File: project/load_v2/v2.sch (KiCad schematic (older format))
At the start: 42 parts, among them P1 CONN_01X02, P2 NGUON, P3 SAC, P4 12N60, P5 CONN_01X02, P6 CONN_01X08, U1 LM7812, U2 7805, U3 ICL7660, U4 TL431

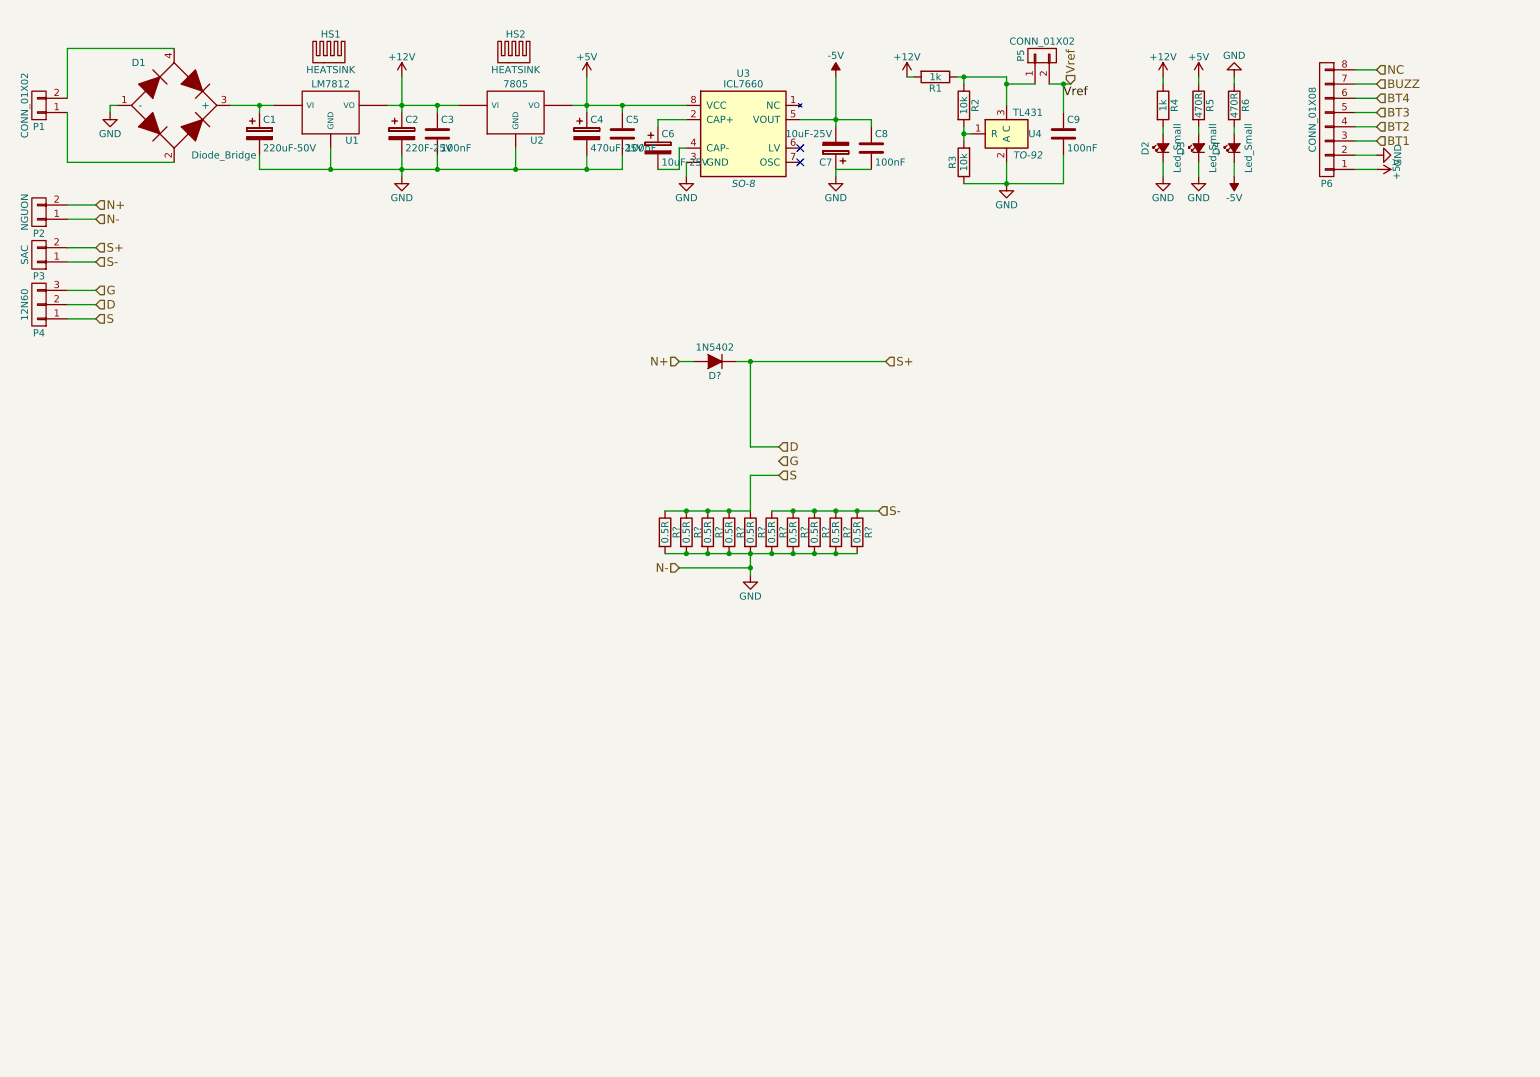
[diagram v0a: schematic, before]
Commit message: schema_load_v2
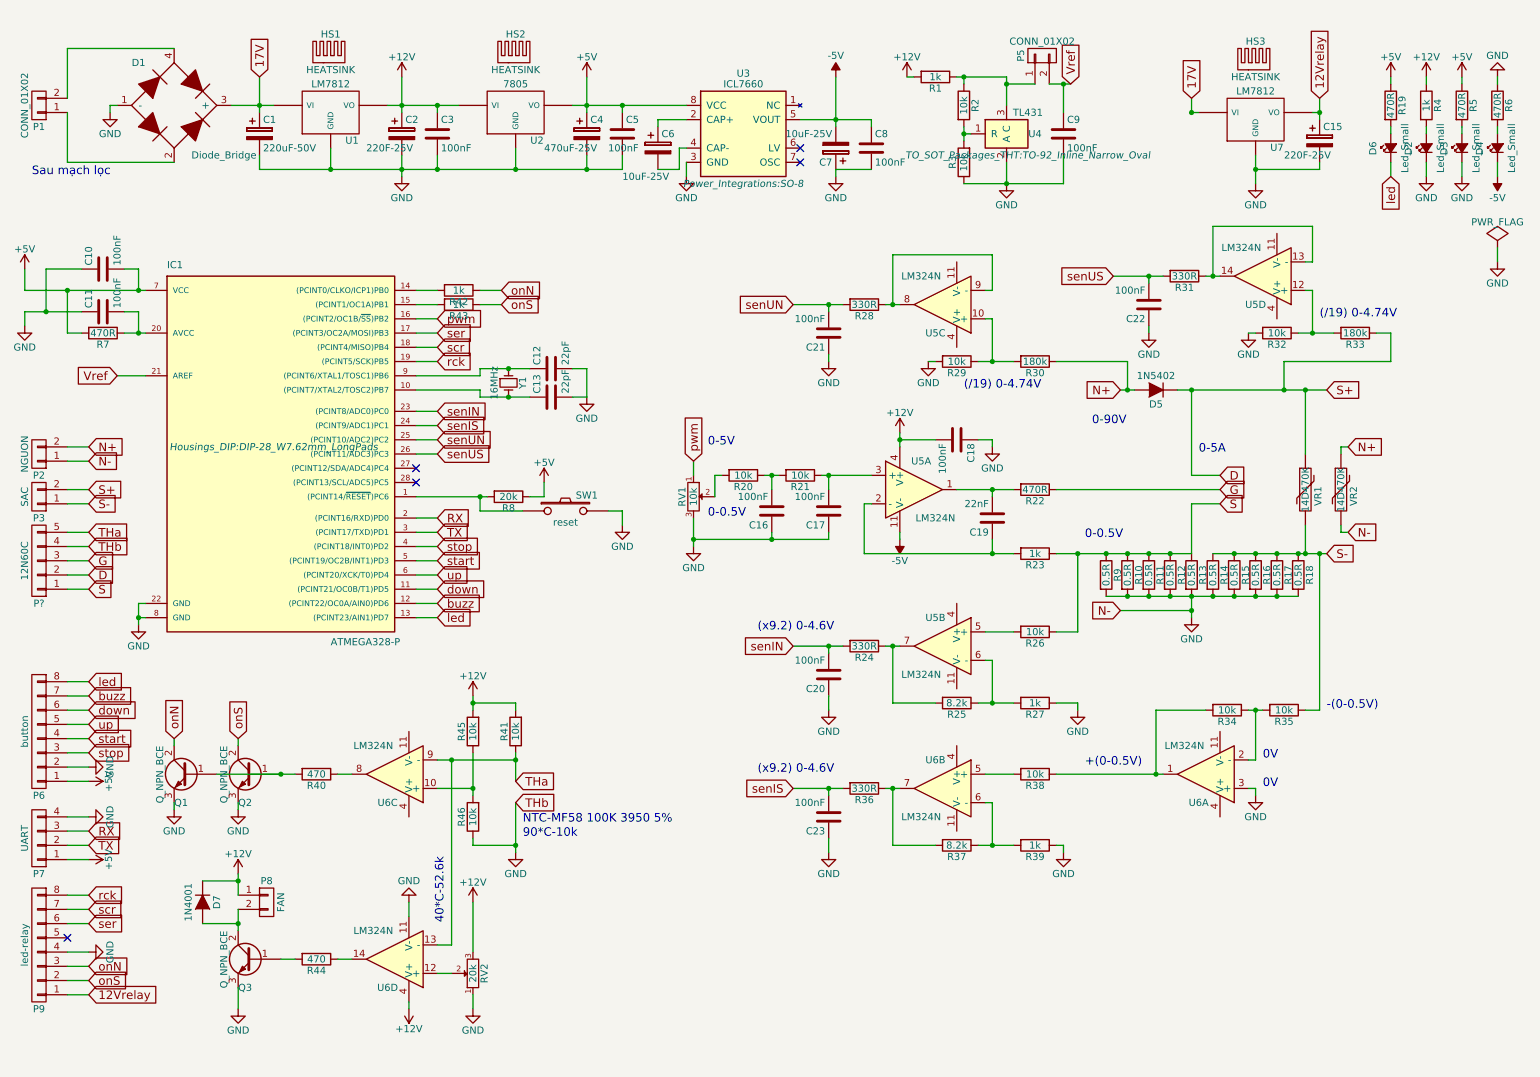
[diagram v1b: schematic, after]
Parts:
- removed P4: 12N60, symbol CONN_01X03
- added C10, C11, C16, C17, C18, C20, C21, C22, C23: 100nF, symbol C
- added C12, C13: 22pF, symbol C
- added C15: 220F-25V, symbol CP
- added C19: 22nF, symbol C
- added D6: Led_Small, symbol Led_Small
- added D7: 1N4001, symbol D
- added HS3: HEATSINK, symbol HEATSINK
- added IC1: ATMEGA328-P, Housings_DIP:DIP-28_W7.62mm_LongPads, symbol ATMEGA328-P
- added P7: UART, symbol CONN_01X04
- added P8: FAN, symbol CONN_01X02
- added P9: led-relay, Socket_Strips:Socket_Strip_Straight_1x08, symbol CONN_01X08
- added P?: 12N60C, symbol CONN_01X05
- added Q1, Q2, Q3: Q_NPN_BCE, symbol Q_NPN_BCE
- added R19, R22, R7: 470R, symbol R
- added R20, R21, R26, R29, R32, R34, R35, R38, R41, R45, R46: 10k, symbol R
- added R23, R27, R39, R42, R43: 1k, symbol R
- added R24, R28, R31, R36: 330R, symbol R
- added R25, R37: 8.2k, symbol R
- added R30, R33: 180k, symbol R
- added R40, R44: 470, symbol R
- added R8: 20k, symbol R
- added RV1: 10k, symbol POT
- added RV2: 20k, symbol POT
- added SW1: reset, symbol SW_PUSH
- added U5, U6: LM324N, symbol LM324N
- added U7: LM7812, symbol LM7812
- added VR1, VR2: 14D470K, symbol VR
- added Y1: 16MHz, Crystals:Crystal_HC52-U_Vertical, symbol Crystal_Small
- P6: value CONN_01X08 -> button; footprint (none) -> Socket_Strips:Socket_Strip_Straight_1x08
- U3: footprint SO-8 -> Power_Integrations:SO-8
- U4: footprint TO-92 -> TO_SOT_Packages_THT:TO-92_Inline_Narrow_Oval
- gave numbers to parts that had none: 11
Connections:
- net +12V: now also C18.2, D7.1 (K), P8.1 (P1), R41.2, R45.2, RV2.3, U5.4 (V+), U6.4 (V+)
- net +5V: now also C10.2, IC1.7 (VCC), P7.1 (P1), R19.1, R7.2, R8.1
- net -5V: now also U5.11 (V-)
- net D: now also P?.2 (P2), R33.1, VR1.1
- net G: now also P?.3 (P3), R22.1
- net GND: now also C10.1, C11.1, C12.2, C13.2, C15.2, C16.1, C17.1, C18.1, C20.1, C21.1, C22.1, C23.1, IC1.22 (GND), IC1.8 (GND), P7.4 (P4), P9.4 (P4), P?.4 (P4), Q1.3 (E), Q2.3 (E), Q3.3 (E), R27.1, R29.2, R32.2, R39.1, R46.1, RV1.3, RV2.1, SW1.2, U6.11 (V-), U6.3 (+), U7.GND, VR2.2
- net N+: now also R30.1, VR2.1
- net S: now also P?.1 (P1), R23.1, R26.1
- net S-: now also R35.1, VR1.2
- net Vref: now also IC1.21 (AREF)
- net 17V: now reaches C1.1, D1.3 (+), U1.VI
- net 17V: now also U7.VI
- net BT1 renamed stop
- net stop: now also IC1.4 ((PCINT18/INT0)PD2)
- net BT2 renamed start
- net start: now also IC1.5 ((PCINT19/OC2B/INT1)PD3)
- net BT3 renamed up
- net up: now also IC1.6 ((PCINT20/XCK/T0)PD4)
- net BT4 renamed down
- net down: now also IC1.11 ((PCINT21/OC0B/T1)PD5)
- net BUZZ renamed buzz
- net buzz: now also IC1.12 ((PCINT22/OC0A/AIN0)PD6)
- net NC renamed led
- net led: now also D6.1 (K), IC1.13 ((PCINT23/AIN1)PD7)
- new net: IC1.1 ((PCINT14/~RESET~)PC6), R8.2, SW1.1
- new net: C13.1, IC1.10 ((PCINT7/XTAL2/TOSC2)PB7), Y1.2
- new net: IC1.14 ((PCINT0/CLKO/ICP1)PB0), R42.2
- new net: IC1.15 ((PCINT1/OC1A)PB1), R43.2
- new net: C11.2, IC1.20 (AVCC), R7.1
- new net: C12.1, IC1.9 ((PCINT6/XTAL1/TOSC1)PB6), Y1.1
- new net: D6.2 (A), R19.2
- new net: C19.2, R22.2, U5.1
- new net: C19.1, R23.2, U5.2 (-)
- new net: C17.2, R21.1, U5.3 (+)
- new net: R26.2, U5.5 (+)
- new net: R25.1, R27.2, U5.6 (-)
- new net: R24.1, R25.2, U5.7
- new net: R29.1, R30.2, U5.10 (+)
- new net: R28.1, U5.8, U5.9 (-)
- new net: R32.1, R33.2, U5.12 (+)
- new net: R31.1, U5.13 (-), U5.14
- new net: R34.2, R38.1, U6.1
- new net: R34.1, R35.2, U6.2 (-)
- new net: R38.2, U6.5 (+)
- new net: R37.1, R39.2, U6.6 (-)
- new net: R36.1, R37.2, U6.7
- new net: R45.1, R46.2, U6.10 (+)
- new net: R40.1, U6.8
- new net: RV2.2, U6.12 (+)
- new net: R44.1, U6.14
- new net: R20.2, RV1.2
- new net: C16.2, R20.1, R21.2
- new net: Q1.1 (B), Q2.1 (B), R40.2
- new net: Q3.1 (B), R44.2
- new net: D7.2 (A), P8.2 (P2), Q3.2 (C)
- new net 12Vrelay: C15.1, P9.1 (P1), U7.VO
- new net RX: IC1.2 ((PCINT16/RXD)PD0), P7.3 (P3)
- new net THa: P?.5 (P5), R41.1, U6.13 (-), U6.9 (-)
- new net TX: IC1.3 ((PCINT17/TXD)PD1), P7.2 (P2)
- new net onN: P9.3 (P3), Q1.2 (C), R42.1
- new net onS: P9.2 (P2), Q2.2 (C), R43.1
- new net pwm: IC1.16 ((PCINT2/OC1B/~SS~)PB2), RV1.1
- new net rck: IC1.19 ((PCINT5/SCK)PB5), P9.8 (P8)
- new net scr: IC1.18 ((PCINT4/MISO)PB4), P9.7 (P7)
- new net senIN: C20.2, IC1.23 ((PCINT8/ADC0)PC0), R24.2
- new net senIS: C23.2, IC1.24 ((PCINT9/ADC1)PC1), R36.2
- new net senUN: C21.2, IC1.25 ((PCINT10/ADC2)PC2), R28.2
- new net senUS: C22.2, IC1.26 ((PCINT11/ADC3)PC3), R31.2
- new net ser: IC1.17 ((PCINT3/OC2A/MOSI)PB3), P9.6 (P6)
- no-connect marks 2 -> 5
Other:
- note added: "(/19) 0-4.74V"
- note added: "(x9.2) 0-4.6V"
- note added: "+(0-0.5V)"
- note added: "-(0-0.5V)"
- note added: "0-0.5V"
- note added: "0-5A"
- note added: "0-5V"
- note added: "0-90V"
- note added: "0V"
- note added: "40*C-52.6k"
- note added: "90*C-10k"
- note added: "NTC-MF58 100K 3950 5%"
- note added: "Sau mạch lọc"
- moved on the sheet: D2, D3, D4, D5, P2, P3, P6, R10, R11, R12, R13, R14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

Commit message: schema_load_v2
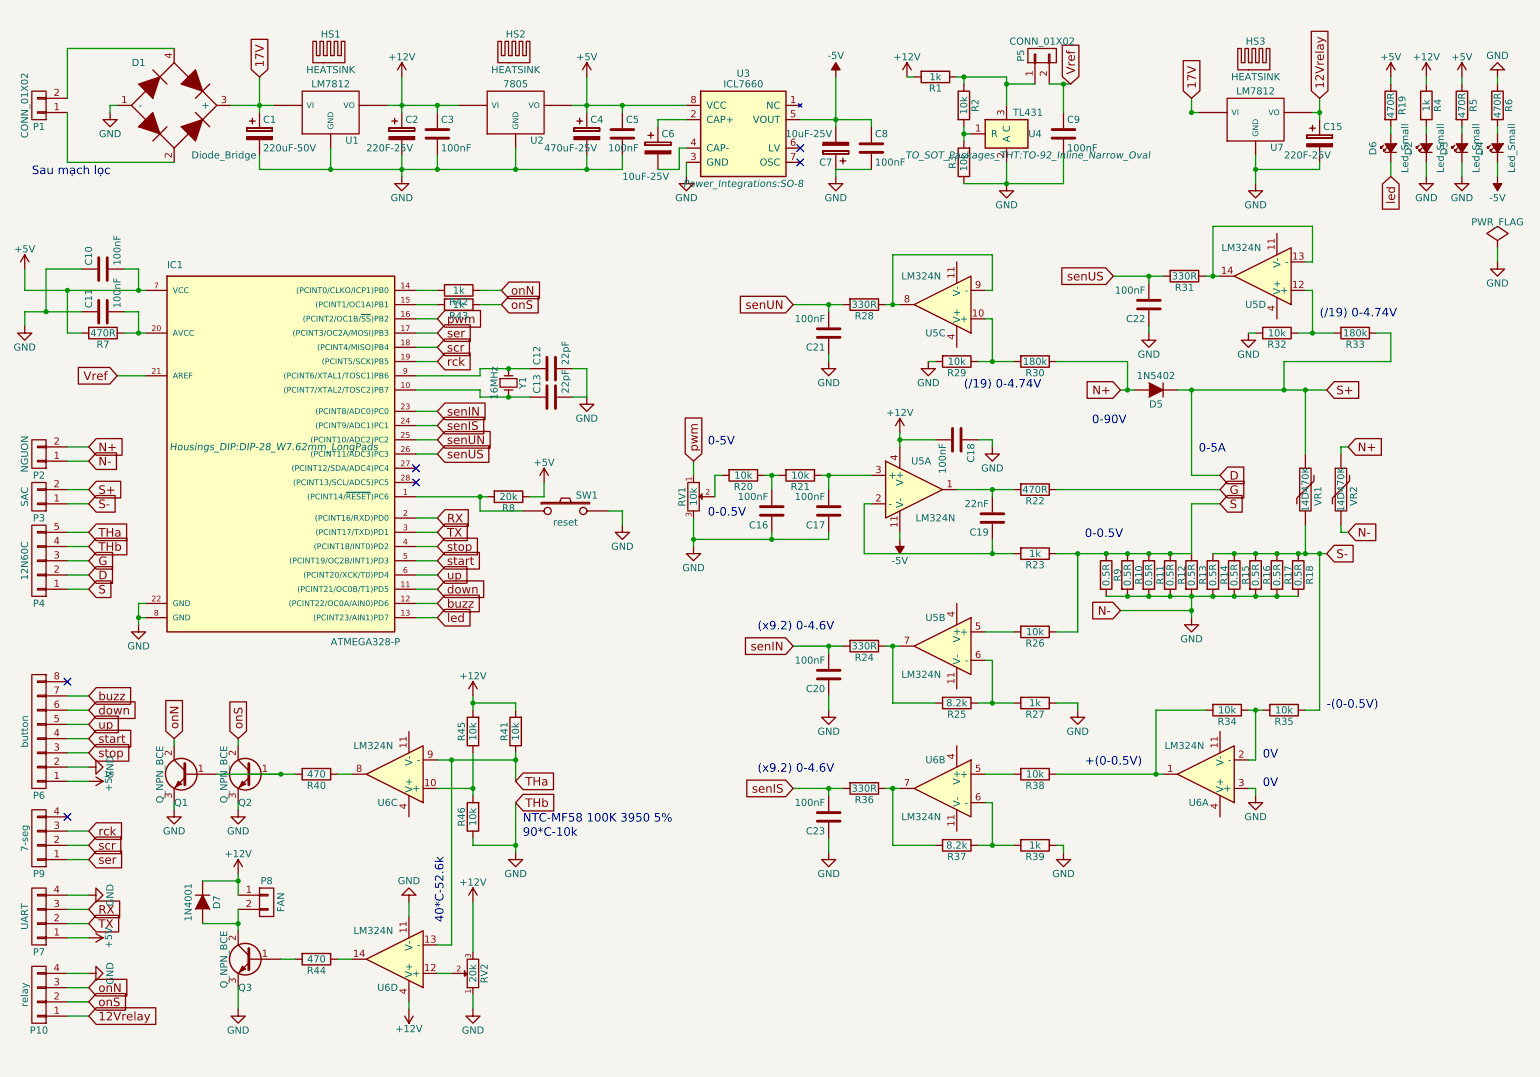
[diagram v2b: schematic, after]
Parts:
- removed P9: led-relay, Socket_Strips:Socket_Strip_Straight_1x08, symbol CONN_01X08
- added P10: relay, symbol CONN_01X04
- added P9: 7-seg, symbol CONN_01X04
- gave numbers to parts that had none: 1
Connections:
- net 12Vrelay: now also P10.1 (P1)
- net GND: now also P10.4 (P4)
- net led: no longer P6.8 (P8)
- net onN: now also P10.3 (P3)
- net onS: now also P10.2 (P2)
- net rck: now also P9.3 (P3)
- net scr: now also P9.2 (P2)
- net ser: now also P9.1 (P1)
- no-connect marks 5 -> 6
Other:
- moved on the sheet: P7

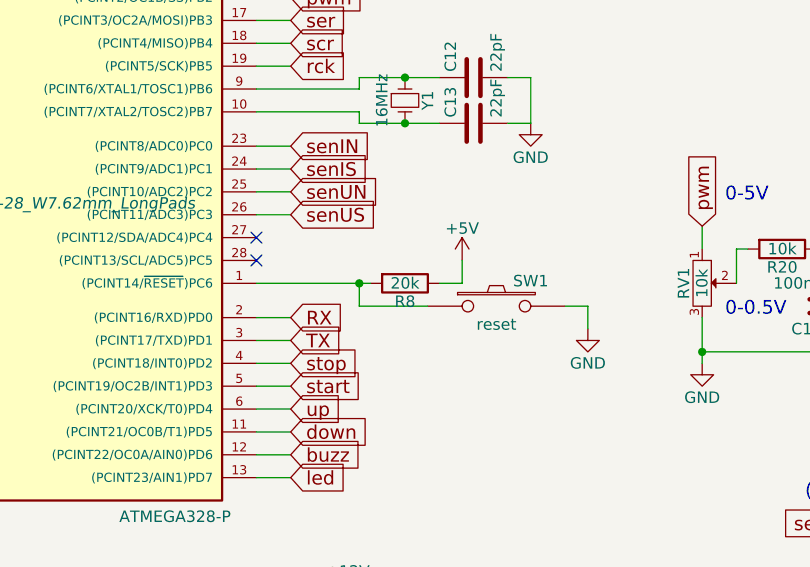
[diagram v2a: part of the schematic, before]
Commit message: schema_load_v2
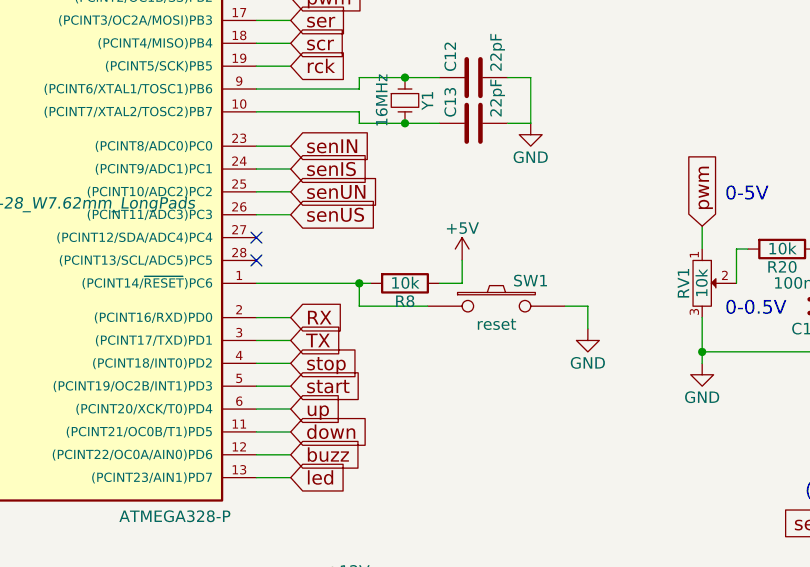
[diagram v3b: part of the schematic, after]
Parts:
- R8: value 20k -> 10k
